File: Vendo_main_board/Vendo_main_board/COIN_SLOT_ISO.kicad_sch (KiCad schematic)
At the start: 56 parts, among them J14 Screw_Terminal_01x03, J15 Screw_Terminal_01x03, J16 Screw_Terminal_01x03, J17 Screw_Terminal_01x03, J18 Screw_Terminal_01x03, J19 Screw_Terminal_01x03, J20 Screw_Terminal_01x03, J21 Screw_Terminal_01x03, U18 PC817, U20 PC817, U21 PC817, U22 PC817, U23 PC817, U24 PC817, U25 PC817, U3 PC817

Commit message: -
added load switch for 12V of coin slot
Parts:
- added C26, C27, C28, C29, C30, C37, C38, C39: 10uF, Capacitor_SMD:C_0603_1608Metric, symbol Device:C
- added C6: 10uF, Capacitor_SMD:C_0805_2012Metric_Pad1.18x1.45mm_HandSolder, symbol Device:C
- added C7: 0.1uF, Capacitor_SMD:C_0603_1608Metric, symbol Device:C
- added Q11, Q13, Q15, Q17, Q19, Q21, Q23, Q25: S8050, Package_TO_SOT_SMD:SOT-23, symbol Transistor_BJT:Q_NPN_BEC
- added Q12, Q14, Q16, Q18, Q20, Q22, Q24, Q26: ~, Footprint Library:SOT-23-3_L2.9-W1.6-P1.90-LS2.8-BR, symbol symbol_library:AO3407A
- added R100, R103, R106, R8, R88, R91, R94, R97: 4.7k, Resistor_SMD:R_0603_1608Metric_Pad0.98x0.95mm_HandSolder, symbol Device:R
- added R101, R104, R107, R89, R9, R92, R95, R98: 100k, Resistor_SMD:R_0603_1608Metric_Pad0.98x0.95mm_HandSolder, symbol Device:R
- added R102, R105, R108, R87, R90, R93, R96, R99: 100, Resistor_SMD:R_0603_1608Metric_Pad0.98x0.95mm_HandSolder, symbol Device:R
- added U5: 74HC595, Package_SO:SOIC-16_3.9x9.9mm_P1.27mm, symbol 74xx:74HC595
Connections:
- net 12V: now also C26.1, C27.1, C28.1, C29.1, C30.1, C37.1, C38.1, C39.1, Q12.2 (S), Q14.2 (S), Q16.2 (S), Q18.2 (S), Q20.2 (S), Q22.2 (S), Q24.2 (S), Q26.2 (S), R101.1, R104.1, R107.1, R89.1, R9.1, R92.1, R95.1, R98.1; no longer J14.1 (Pin_1), J15.1 (Pin_1), J16.1 (Pin_1), J17.1 (Pin_1), J18.1 (Pin_1), J19.1 (Pin_1), J20.1 (Pin_1), J21.1 (Pin_1)
- net GNDD: now also C6.1, C7.1, U5.13 (~{OE}), U5.8 (GND)
- net GNDPWR: now also C26.2, C27.2, C28.2, C29.2, C30.2, C37.2, C38.2, C39.2, Q11.2 (E), Q13.2 (E), Q15.2 (E), Q17.2 (E), Q19.2 (E), Q21.2 (E), Q23.2 (E), Q25.2 (E)
- new net: Q15.1 (B), R91.2
- new net: Q23.1 (B), R103.2
- new net: Q19.1 (B), R97.2
- new net: Q19.3 (C), R98.2, R99.1
- new net: Q11.3 (C), R87.1, R9.2
- new net: Q12.1 (G), R87.2
- new net: Q20.1 (G), R99.2
- new net: Q13.3 (C), R89.2, R90.1
- new net: Q22.1 (G), R102.2
- new net: Q15.3 (C), R92.2, R93.1
- new net: Q14.1 (G), R90.2
- new net: Q25.1 (B), R106.2
- new net: Q11.1 (B), R8.2
- new net: Q21.3 (C), R101.2, R102.1
- new net: Q13.1 (B), R88.2
- new net: Q18.1 (G), R96.2
- new net: Q21.1 (B), R100.2
- new net: Q16.1 (G), R93.2
- new net: Q17.3 (C), R95.2, R96.1
- new net: Q23.3 (C), R104.2, R105.1
- new net: Q24.1 (G), R105.2
- new net: Q17.1 (B), R94.2
- new net: Q26.1 (G), R108.2
- new net: Q25.3 (C), R107.2, R108.1
- new net +5V: C6.2, C7.2, U5.10 (~{SRCLR}), U5.16 (VCC)
- new net 12VA: J14.1 (Pin_1), Q12.3 (D)
- new net 12VB: J16.1 (Pin_1), Q14.3 (D)
- new net 12VC: J18.1 (Pin_1), Q16.3 (D)
- new net 12VD: J20.1 (Pin_1), Q18.3 (D)
- new net 12VE: J15.1 (Pin_1), Q26.3 (D)
- new net 12VF: J17.1 (Pin_1), Q24.3 (D)
- new net 12VG: J19.1 (Pin_1), Q22.3 (D)
- new net 12VH: J21.1 (Pin_1), Q20.3 (D)
- new net QA: R8.1, U5.15 (QA)
- new net QB: R88.1, U5.1 (QB)
- new net QC: R91.1, U5.2 (QC)
- new net QD: R94.1, U5.3 (QD)
- new net QE: R106.1, U5.4 (QE)
- new net QF: R103.1, U5.5 (QF)
- new net QG: R100.1, U5.6 (QG)
- new net QH: R97.1, U5.7 (QH)
- new net REG_CLK: U5.11 (SRCLK)
- new net REG_CS: U5.12 (RCLK)
- new net SHIT_REG2: U5.14 (SER)
- no-connect marks 0 -> 1
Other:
- note added: "D"
- note added: "G"
- note added: "S"
- moved on the sheet: J14, J15, J16, J17, J18, J19, J20, J21, R10, R11, R12, R13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

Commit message: -update schematic
-recheck lcsc part number ,value
-check and update footprint assignment
-add load switch for the wdt and ldo combination

-add link for quick connect footprint must be discuss for clarification
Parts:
- C26, C27, C28, C29, C30, C37, C38, C39: footprint Capacitor_SMD:C_0603_1608Metric -> Capacitor_SMD:C_0805_2012Metric_Pad1.18x1.45mm_HandSolder; LCSC C107088 -> C15850
- Q12, Q14, Q16, Q18, Q20, Q22, Q24, Q26: footprint Footprint Library:SOT-23-3_L2.9-W1.6-P1.90-LS2.8-BR -> footprints:SOT-23-3_L2.9-W1.6-P1.90-LS2.8-BR
- R100, R103, R106, R8, R88, R91, R94, R97: LCSC C881308 -> C99782
- R101, R104, R107, R89, R9, R92, R95, R98: LCSC C881308 -> C14675
- R102, R105, R108, R87, R90, R93, R96, R99: LCSC C881308 -> C193336
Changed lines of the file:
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@@
 			)
 		)
-		(property "LCSC" "C881308"
+		(property "LCSC" "C99782"
 			(at 324.309 194.773 0)
 			(effects
@@
 			)
 		)
-		(property "LCSC" "C881308"
+		(property "LCSC" "C99782"
 			(at 221.3899 329.35 0)
 			(effects
@@
 			)
 		)
-		(property "Footprint" "Capacitor_SMD:C_0603_1608Metric"
+		(property "Footprint" "Capacitor_SMD:C_0805_2012Metric_Pad1.18x1.45mm_HandSolder"
 			(at 431.4195 311.9454 0)
 			(effects
@@
 			)
 		)
-		(property "LCSC" "C107088"
+		(property "LCSC" "C15850"
 			(at 430.4543 308.1354 0)
 			(effects
@@
 			)
 		)
-		(property "LCSC" "C881308"
+		(property "LCSC" "C193336"
 			(at 154.1428 186.4222 0)
 			(effects
@@
 			)
 		)
-		(property "Footprint" "Capacitor_SMD:C_0603_1608Metric"
+		(property "Footprint" "Capacitor_SMD:C_0805_2012Metric_Pad1.18x1.45mm_HandSolder"
 			(at 332.5772 308.9502 0)
 			(effects
@@
 			)
 		)
-		(property "LCSC" "C107088"
+		(property "LCSC" "C15850"
 			(at 331.612 305.1402 0)
 			(effects
@@
 			)
 		)
-		(property "LCSC" "C881308"
+		(property "LCSC" "C193336"
 			(at 446.2411 321.8357 0)
 			(effects
@@
 			)
 		)
-		(property "LCSC" "C881308"
+		(property "LCSC" "C14675"
 			(at 244.2787 175.1345 0)
 			(effects
@@
 			)
 		)
-		(property "Footprint" "Capacitor_SMD:C_0603_1608Metric"
+		(property "Footprint" "Capacitor_SMD:C_0805_2012Metric_Pad1.18x1.45mm_HandSolder"
 			(at 333.2844 176.2452 0)
 			(effects
@@
 			)
 		)
-		(property "LCSC" "C107088"
+		(property "LCSC" "C15850"
 			(at 332.3192 172.4352 0)
 			(effects
@@
 			)
 		)
-		(property "Footprint" "Footprint Library:SOT-23-3_L2.9-W1.6-P1.90-LS2.8-BR"
+		(property "Footprint" "footprints:SOT-23-3_L2.9-W1.6-P1.90-LS2.8-BR"
 			(at 339.268 304.1242 0)
 			(effects
@@
 			)
 		)
-		(property "Footprint" "Capacitor_SMD:C_0603_1608Metric"
+		(property "Footprint" "Capacitor_SMD:C_0805_2012Metric_Pad1.18x1.45mm_HandSolder"
 			(at 139.3212 176.5319 0)
 			(effects
@@
 			)
 		)
-		(property "LCSC" "C107088"
+		(property "LCSC" "C15850"
 			(at 138.356 172.7219 0)
 			(effects
@@
 			)
 		)
-		(property "LCSC" "C881308"
+		(property "LCSC" "C193336"
 			(at 248.9309 186.9675 0)
 			(effects
@@
 			)
 		)
-		(property "LCSC" "C881308"
+		(property "LCSC" "C99782"
 			(at 128.1636 326.3548 0)
 			(effects
@@
 			)
 		)
-		(property "LCSC" "C881308"
+		(property "LCSC" "C99782"
 			(at 130.3458 195.0597 0)
 			(effects
@@
 			)
 		)
-		(property "LCSC" "C881308"
+		(property "LCSC" "C193336"
 			(at 347.3988 318.8405 0)
 			(effects
@@
 			)
 		)
-		(property "LCSC" "C881308"
+		(property "LCSC" "C99782"
 			(at 422.4441 330.4732 0)
 			(effects
@@
 			)
 		)
-		(property "LCSC" "C881308"
+		(property "LCSC" "C14675"
 			(at 342.7466 307.0075 0)
 			(effects
@@
 			)
 		)
-		(property "LCSC" "C881308"
+		(property "LCSC" "C99782"
 			(at 225.1339 195.605 0)
 			(effects
@@
 			)
 		)
-		(property "Footprint" "Footprint Library:SOT-23-3_L2.9-W1.6-P1.90-LS2.8-BR"
+		(property "Footprint" "footprints:SOT-23-3_L2.9-W1.6-P1.90-LS2.8-BR"
 			(at 438.1103 307.1194 0)
 			(effects
@@
 			)
 		)
-		(property "Footprint" "Footprint Library:SOT-23-3_L2.9-W1.6-P1.90-LS2.8-BR"
+		(property "Footprint" "footprints:SOT-23-3_L2.9-W1.6-P1.90-LS2.8-BR"
 			(at 439.608 174.9552 0)
 			(effects
@@
 			)
 		)
-		(property "LCSC" "C881308"
+		(property "LCSC" "C193336"
 			(at 348.106 186.1355 0)
 			(effects
@@
 			)
 		)
-		(property "LCSC" "C881308"
+		(property "LCSC" "C14675"
 			(at 441.5889 310.0027 0)
 			(effects
@@
 			)
 		)
-		(property "LCSC" "C881308"
+		(property "LCSC" "C14675"
 			(at 343.4538 174.3025 0)
 			(effects
@@
 			)
 		)
-		(property "LCSC" "C881308"
+		(property "LCSC" "C14675"
 			(at 149.4906 174.5892 0)
 			(effects
@@
 			)
 		)
-		(property "Footprint" "Capacitor_SMD:C_0603_1608Metric"
+		(property "Footprint" "Capacitor_SMD:C_0805_2012Metric_Pad1.18x1.45mm_HandSolder"
 			(at 137.139 307.827 0)
 			(effects
@@
 			)
 		)
-		(property "LCSC" "C107088"
+		(property "LCSC" "C15850"
 			(at 136.1738 304.017 0)
 			(effects
@@
 			)
 		)
-		(property "Footprint" "Capacitor_SMD:C_0603_1608Metric"
+		(property "Footprint" "Capacitor_SMD:C_0805_2012Metric_Pad1.18x1.45mm_HandSolder"
 			(at 230.3653 310.8222 0)
 			(effects
@@
 			)
 		)
-		(property "LCSC" "C107088"
+		(property "LCSC" "C15850"
 			(at 229.4001 307.0122 0)
 			(effects
@@
 			)
 		)
-		(property "LCSC" "C881308"
+		(property "LCSC" "C14675"
 			(at 443.0866 177.8385 0)
 			(effects
@@
 			)
 		)
-		(property "LCSC" "C881308"
+		(property "LCSC" "C193336"
 			(at 245.1869 320.7125 0)
 			(effects
@@
 			)
 		)
-		(property "LCSC" "C881308"
+		(property "LCSC" "C99782"
 			(at 423.9418 198.309 0)
 			(effects
@@
 			)
 		)
-		(property "Footprint" "Footprint Library:SOT-23-3_L2.9-W1.6-P1.90-LS2.8-BR"
+		(property "Footprint" "footprints:SOT-23-3_L2.9-W1.6-P1.90-LS2.8-BR"
 			(at 143.8298 303.001 0)
 			(effects
@@
 			)
 		)
-		(property "LCSC" "C881308"
+		(property "LCSC" "C99782"
 			(at 323.6018 327.478 0)
 			(effects
@@
 			)
 		)
-		(property "Footprint" "Footprint Library:SOT-23-3_L2.9-W1.6-P1.90-LS2.8-BR"
+		(property "Footprint" "footprints:SOT-23-3_L2.9-W1.6-P1.90-LS2.8-BR"
 			(at 146.012 171.7059 0)
 			(effects
@@
 			)
 		)
-		(property "Footprint" "Footprint Library:SOT-23-3_L2.9-W1.6-P1.90-LS2.8-BR"
+		(property "Footprint" "footprints:SOT-23-3_L2.9-W1.6-P1.90-LS2.8-BR"
 			(at 237.0561 305.9962 0)
 			(effects
@@
 			)
 		)
-		(property "Footprint" "Capacitor_SMD:C_0603_1608Metric"
+		(property "Footprint" "Capacitor_SMD:C_0805_2012Metric_Pad1.18x1.45mm_HandSolder"
 			(at 432.9172 179.7812 0)
 			(effects
@@
 			)
 		)
-		(property "LCSC" "C107088"
+		(property "LCSC" "C15850"
 			(at 431.952 175.9712 0)
 			(effects
@@
 			)
 		)
-		(property "LCSC" "C881308"
+		(property "LCSC" "C193336"
 			(at 151.9606 317.7173 0)
 			(effects
@@
 			)
 		)
-		(property "LCSC" "C881308"
+		(property "LCSC" "C193336"
 			(at 447.7388 189.6715 0)
 			(effects
@@
 			)
 		)
-		(property "LCSC" "C881308"
+		(property "LCSC" "C14675"
 			(at 147.3084 305.8843 0)
 			(effects
@@
 			)
 		)
-		(property "Footprint" "Footprint Library:SOT-23-3_L2.9-W1.6-P1.90-LS2.8-BR"
+		(property "Footprint" "footprints:SOT-23-3_L2.9-W1.6-P1.90-LS2.8-BR"
 			(at 339.9752 171.4192 0)
 			(effects
@@
 			)
 		)
-		(property "Footprint" "Footprint Library:SOT-23-3_L2.9-W1.6-P1.90-LS2.8-BR"
+		(property "Footprint" "footprints:SOT-23-3_L2.9-W1.6-P1.90-LS2.8-BR"
 			(at 240.8001 172.2512 0)
 			(effects
@@
 			)
 		)
-		(property "LCSC" "C881308"
+		(property "LCSC" "C14675"
 			(at 240.5347 308.8795 0)
 			(effects
@@
 			)
 		)
-		(property "Footprint" "Capacitor_SMD:C_0603_1608Metric"
+		(property "Footprint" "Capacitor_SMD:C_0805_2012Metric_Pad1.18x1.45mm_HandSolder"
 			(at 234.1093 177.0772 0)
 			(effects
@@
 			)
 		)
-		(property "LCSC" "C107088"
+		(property "LCSC" "C15850"
 			(at 233.1441 173.2672 0)
 			(effects

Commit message: -update scheme and pcb placement
update scheme and footprint
added spade connectors
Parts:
- J10: renamed from J18; footprint (none) -> Connector_JST:JST_EH_B3B-EH-A_1x03_P2.50mm_Vertical
- J11: renamed from J21; footprint (none) -> Connector_JST:JST_EH_B3B-EH-A_1x03_P2.50mm_Vertical
- J12: renamed from J20; footprint (none) -> Connector_JST:JST_EH_B3B-EH-A_1x03_P2.50mm_Vertical
- J5: renamed from J15; footprint (none) -> Connector_JST:JST_EH_B3B-EH-A_1x03_P2.50mm_Vertical
- J6: renamed from J14; footprint (none) -> Connector_JST:JST_EH_B3B-EH-A_1x03_P2.50mm_Vertical
- J7: renamed from J17; footprint (none) -> Connector_JST:JST_EH_B3B-EH-A_1x03_P2.50mm_Vertical
- J8: renamed from J16; footprint (none) -> Connector_JST:JST_EH_B3B-EH-A_1x03_P2.50mm_Vertical
- J9: renamed from J19; footprint (none) -> Connector_JST:JST_EH_B3B-EH-A_1x03_P2.50mm_Vertical
- renumbered C6 to C32, C7 to C33, C39 to C34, C28 to C35, C38 to C36, C26 to C37, C37 to C38, C27 to C39, C30 to C40, C29 to C41, Q14 to Q10, Q21 to Q11, Q15 to Q12, Q22 to Q13, Q16 to Q14, Q19 to Q15, Q17 to Q16, Q20 to Q17, Q25 to Q3, Q11 to Q4, Q26 to Q5, Q12 to Q6, Q23 to Q7, Q13 to Q8, Q24 to Q9, R11 to R22, R14 to R23, R63 to R24, R64 to R25, R106 to R26, R8 to R27, R80 to R28, R79 to R29, R107 to R30, R9 to R31, R108 to R32, R87 to R33, R43 to R34, R56 to R35, R10 to R36, R55 to R37, R103 to R38, R88 to R39, R65 to R40, R66 to R41, R57 to R42, R58 to R43, R82 to R44, R81 to R45, R104 to R46, R89 to R47, R105 to R48, R90 to R49, R69 to R50, R70 to R51, R67 to R52, R68 to R53, R15 to R54, R16 to R55, R100 to R56, R91 to R57, R12 to R58, R13 to R59, R84 to R60, R83 to R61, R101 to R62, R92 to R63, R102 to R64, R93 to R65, R61 to R66, R62 to R67, R59 to R68, R60 to R69, R97 to R70, R94 to R71, R73 to R72, R74 to R73, R71 to R74, R72 to R75, R86 to R76, R85 to R77, R98 to R78, R95 to R79, R99 to R80, R96 to R81, R77 to R82, R78 to R83, R75 to R84, R76 to R85, U5 to U10, U3 to U11, U20 to U12, U22 to U13, U21 to U14, U23 to U15, U18 to U16, U25 to U17, U24 to U18

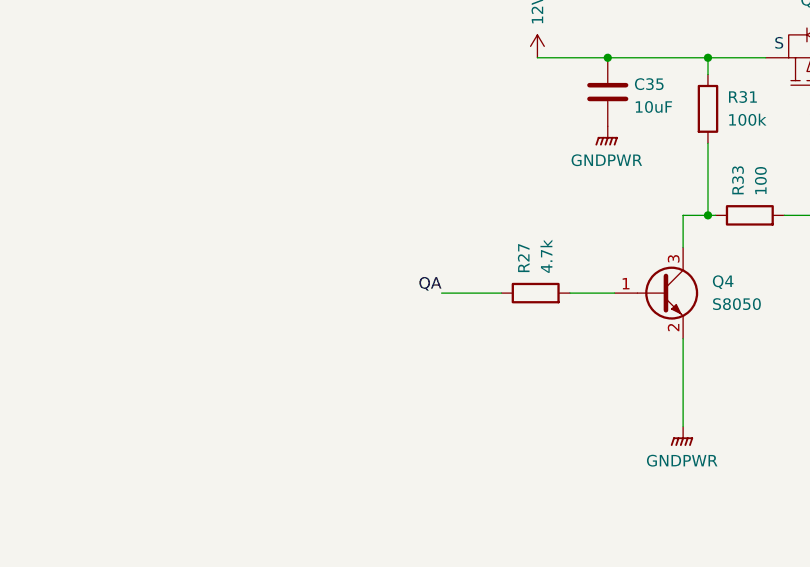
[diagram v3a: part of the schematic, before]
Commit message: -update scheme for modular design
-12V to 5V buck
-5V isolation
-3v3 ldo with wdt
-STM32 blue pill
-dip switch 8 pos with 74HC165
-built in type C programmer
-STLINK 1x4 provisioned
-seven segment port with TM1637 (DIO,CLK)
-relay with 10A & 30A provision , spade connector is put on choosing between 12V supply or external supply , as well on the Common of relay for Ground option
-Coin slot with opto, and loadswitch for it supply 3 pin jst for the port
-slave connector 6 pin jst ,i2c ,5V input for slave seperate gnds
-terminal block for 12V selector for ease of wiring for multiple boards
-terminal io blocks are 16 pin
1button and led with ground pair
12V supply for  device and external supply with grnd pair
relay nc,no and com
esp interrup,sda,scl and gnd for iot connection
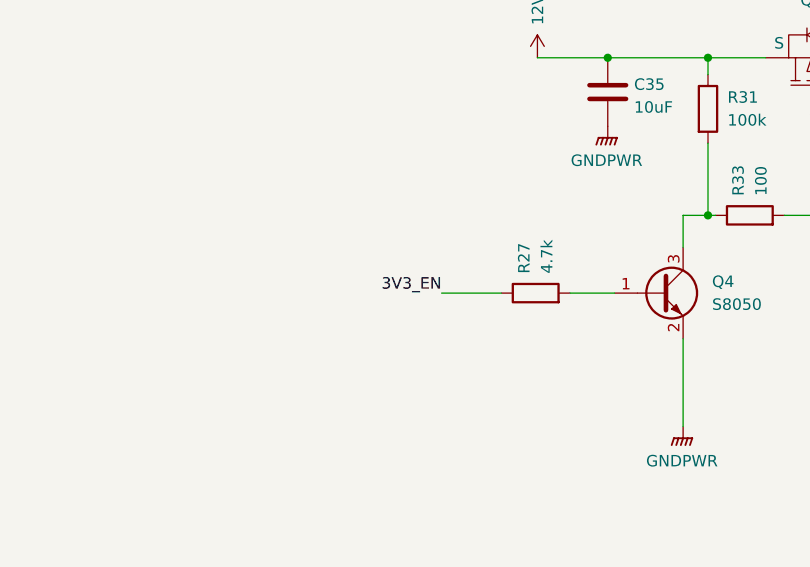
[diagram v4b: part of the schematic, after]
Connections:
- net QA: no longer R27.1
- new net 3V3_EN: R27.1
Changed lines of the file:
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@@
 		)
 	)
-	(label "QA"
+	(label "3V3_EN"
 		(at 119.8905 195.0597 180)
 		(effects
